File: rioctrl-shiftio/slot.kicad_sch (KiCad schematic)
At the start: 8 parts, among them J1 Conn_02x13_Odd_Even, Q1 BSS138W

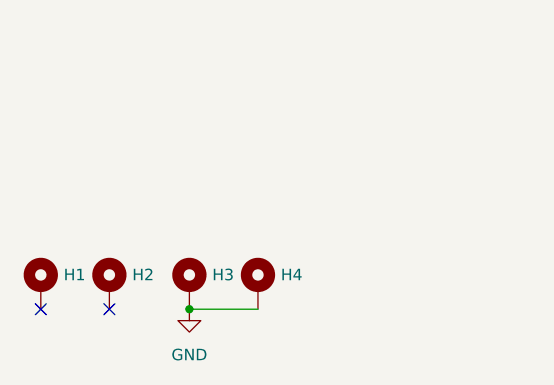
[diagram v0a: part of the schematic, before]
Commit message: Fill in BOM (LCSC#)
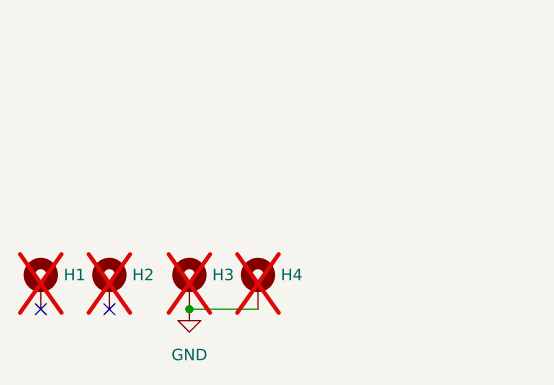
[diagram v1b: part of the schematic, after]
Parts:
- H1, H2, H3, H4: now not fitted
- J1: LCSC# (none) -> C2894993
- R1: LCSC# (none) -> C98220
- R2: LCSC# (none) -> C99782
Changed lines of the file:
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@@
 		(in_bom no)
 		(on_board yes)
-		(dnp no)
+		(dnp yes)
 		(fields_autoplaced yes)
 		(property "Reference" "H2"
@@
 		(in_bom no)
 		(on_board yes)
-		(dnp no)
+		(dnp yes)
 		(fields_autoplaced yes)
 		(property "Reference" "H4"
@@
 		(in_bom no)
 		(on_board yes)
-		(dnp no)
+		(dnp yes)
 		(fields_autoplaced yes)
 		(property "Reference" "H3"
@@
 		)
 		(property "Description" "Generic connector, double row, 02x13, odd/even pin numbering scheme (row 1 odd numbers, row 2 even numbers), script generated (kicad-library-utils/schlib/autogen/connector/)"
+			(at 120.65 88.9 0)
+			(effects
+				(font
+					(size 1.27 1.27)
+				)
+				(hide yes)
+			)
+		)
+		(property "LCSC#" "C2894993"
 			(at 120.65 88.9 0)
 			(effects
@@
 			)
 		)
+		(property "LCSC#" "C98220"
+			(at 168.91 130.81 0)
+			(effects
+				(font
+					(size 1.27 1.27)
+				)
+				(hide yes)
+			)
+		)
 		(pin "1"
 		)
@@
 		(in_bom no)
 		(on_board yes)
-		(dnp no)
+		(dnp yes)
 		(fields_autoplaced yes)
 		(property "Reference" "H1"
@@
 			(at 179.07 113.03 0)
 			(effects
+				(font
+					(size 1.27 1.27)
+				)
+				(hide yes)
+			)
+		)
+		(property "LCSC#" "C99782"
+			(at 179.07 113.03 0)
+			(effects
